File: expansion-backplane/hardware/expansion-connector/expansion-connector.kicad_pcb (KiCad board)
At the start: 2 copper layers, 39 x 45 mm, 2 parts

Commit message: updatedd PCB layouts
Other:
- board text added: "Minimal 64x4 Expansion Bus Connector"
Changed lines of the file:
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@@
 		(layer "Edge.Cuts")
+	)
+	(gr_text "Minimal 64x4\nExpansion Bus Connector"
+		(at 144.5 97.5 90)
+		(layer "F.SilkS")
+		(effects
+			(font
+				(size 1.7 1.5)
+				(thickness 0.2)
+			)
+		)
 	)
 	(segment

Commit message: update speech pld file and more
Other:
- board text added: "To Back -->"
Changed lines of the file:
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@@
 			(outputformat 1)
 			(mirror no)
-			(drillshape 1)
+			(drillshape 0)
 			(scaleselection 1)
-			(outputdirectory "")
+			(outputdirectory "gerbers_v1")
 		)
 	)
@@
 		)
 	)
+	(gr_text "To Back -->"
+		(at 156.21 84.328 90)
+		(layer "F.SilkS")
+		(effects
+			(font
+				(size 0.8 0.8)
+				(thickness 0.1)
+			)
+			(justify left bottom)
+		)
+	)

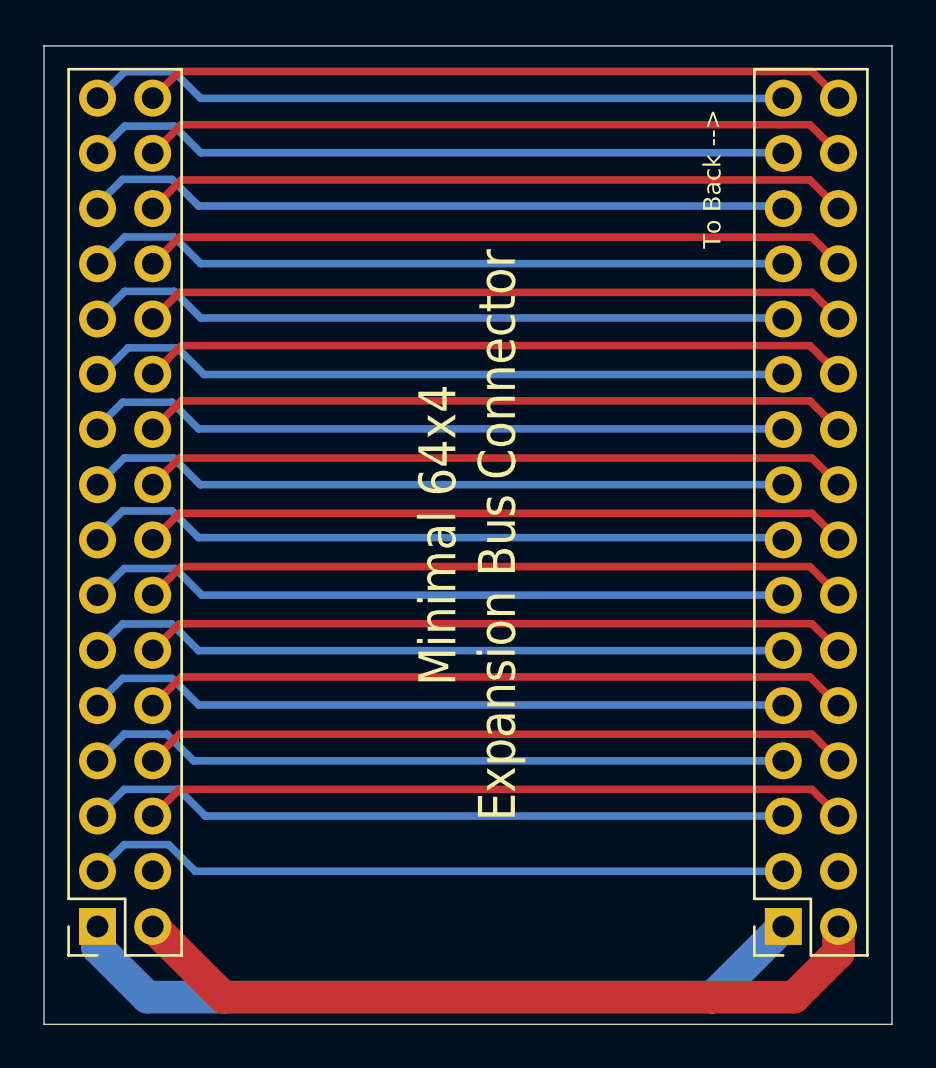
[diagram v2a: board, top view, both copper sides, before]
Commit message: Hardware Multiplier (#1)
Created a hardware multiplier for the Minimal 64x4
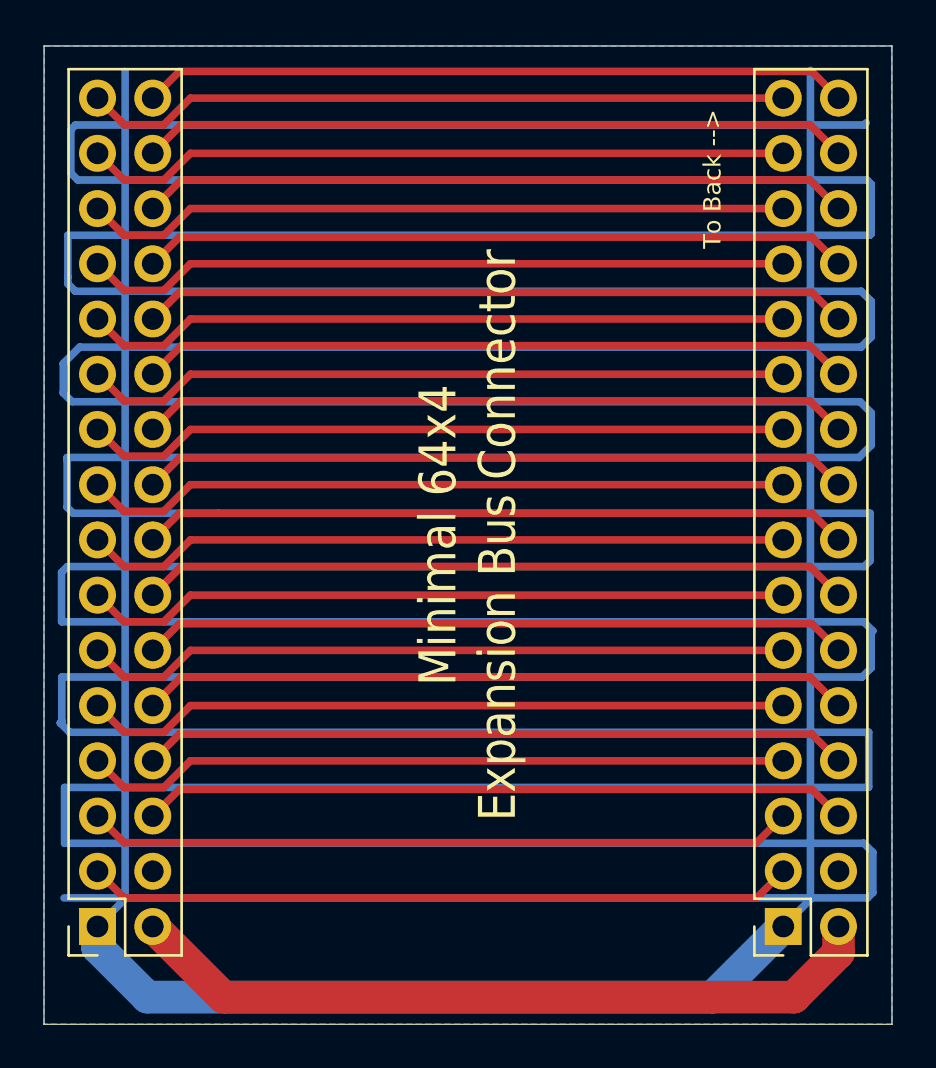
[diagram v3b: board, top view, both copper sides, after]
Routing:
- net GND: track 34.8 -> 701.8 mm
- added copper zone on B.Cu, net GND
